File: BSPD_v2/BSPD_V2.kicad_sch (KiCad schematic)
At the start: 13 parts, among them K1 G5V-1, P1 0430450827, T1 T-BJT-NPN, U1 SN74HC00N, U2 LM393P, U3 LM393P, U4 LM393P, U5 SN74HC08N

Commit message: updated schematic
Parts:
- added C1, C2: C_Generic, Capacitor_THT:C_Disc_D12.5mm_W5.0mm_P10.00mm, symbol PCM_4ms_Capacitor:C_Generic
- added D1, D2, D3: LED, LED_THT:LED_D5.0mm_Horizontal_O6.35mm_Z9.0mm, symbol Device:LED
- added R1, R2, R3, R4, R5: R, PCM_Resistor_THT_AKL:R_Axial_DIN0918_L18.0mm_D9.0mm_P25.40mm_Horizontal, symbol Device:R
- added U6: LM2596T-5, PCM_Package_TO_SOT_THT_AKL:TO-220F-5_P3.4x2.06mm_StaggerEven_Lead1.86mm_Vertical, symbol Regulator_Switching:LM2596T-5
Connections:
- net +5V: now also U3.8 (VCC)
- net GND: now also P1.7, C1.2, C2.2, D1.1 (K), D2.1 (K), D3.1 (K)
- net at TRIM4.2 (Center): now also U4.3 (1IN+)
- net at U4.1 (1OUT): now also U5.5 (2B)
- net at U4.2 (1IN-): now also C1.1, R1.1
- net at U4.5 (2IN+): now also TRIM5.2 (Center)
- net at U4.6 (2IN-): now also C2.1, R2.1
- net at U4.7 (2OUT): now also U5.4 (2A)
- net IN: now reaches K1.10
- net at K1.2: now also T1.3 (E)
- net OUT: now reaches K1.5, K1.6
- net at U1.1 (1A): now also U2.1 (1OUT)
- net at U1.2 (1B): now also U3.1 (1OUT)
- net at U1.3 (1Y): now also R1.2
- net BPS_sensor: now reaches U3.2 (1IN-)
- net BPS_sensor: now also P1.2, U3.6 (2IN-), R4.2
- net at U3.5 (2IN+): now also TRIM3.2 (Center), U2.5 (2IN+)
- net at U3.7 (2OUT): now also U5.2 (1B)
- net TPS_sensor: now reaches P1.1
- net TPS_sensor: now also U2.2 (1IN-), U2.6 (2IN-), R5.2
- net at P1.8: now also U6.2 (OUT)
- net at T1.2 (B): now also U5.6 (2Y)
- net at U2.7 (2OUT): now also U5.1 (1A)
- net at U5.3 (1Y): now also R2.2
- new net: D3.2 (A), R3.1
- new net: D2.2 (A), R4.1
- new net: D1.2 (A), R5.1
- new net +12V: U6.1 (VIN)
- no-connect marks 0 -> 2
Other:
- moved on the sheet: P1, T1, TRIM2, TRIM3, TRIM4, TRIM5, U4, U5

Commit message: updated schematic
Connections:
- net GND: now also U6.3 (GND); no longer P1.7
- net at P1.8, U6.2 (OUT): now also R3.2
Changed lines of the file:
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@@
+	)
+	(junction
+		(at 45.72 175.26)
+		(diameter 0)
+		(color 0 0 0 0)
 	)
 	(junction
@@
 	(wire
 		(pts
-			(xy 43.18 173.99) (xy 43.18 175.26)
+			(xy 127 173.99) (xy 128.27 173.99)
 		)
 		(stroke
@@
 		(pts
 			(xy 66.04 181.61) (xy 66.04 194.31)
+		)
+		(stroke
+			(width 0)
+			(type default)
+		)
+	)
+	(wire
+		(pts
+			(xy 45.72 175.26) (xy 45.72 191.77)
 		)
 		(stroke
@@
 	(symbol
 		(lib_id "PCM_4ms_Power-symbol:GND")
-		(at 43.18 173.99 180)
+		(at 127 173.99 270)
 		(unit 1)
 		(exclude_from_sim no)
@@
 		(on_board yes)
 		(dnp no)
-		(fields_autoplaced yes)
 		(property "Reference" "#PWR026"
-			(at 43.18 167.64 0)
+			(at 120.65 173.99 0)
 			(effects
 				(font
@@
 		)
 		(property "Value" "GND"
-			(at 43.18 168.91 0)
+			(at 123.19 173.99 0)
 			(effects
 				(font
@@
 		)
 		(property "Footprint" ""
-			(at 43.18 173.99 0)
+			(at 127 173.99 0)
 			(effects
 				(font
@@
 		)
 		(property "Datasheet" ""
-			(at 43.18 173.99 0)
+			(at 127 173.99 0)
 			(effects
 				(font
@@
 		)
 		(property "Description" ""
-			(at 43.18 173.99 0)
+			(at 127 173.99 0)
 			(effects
 				(font
@@
 		)
 		(instances
-			(project ""
+			(project "BSPD_v2"
 				(path "/382198d7-19bb-422e-88d5-5462e049fe29"
 					(reference "#PWR026")

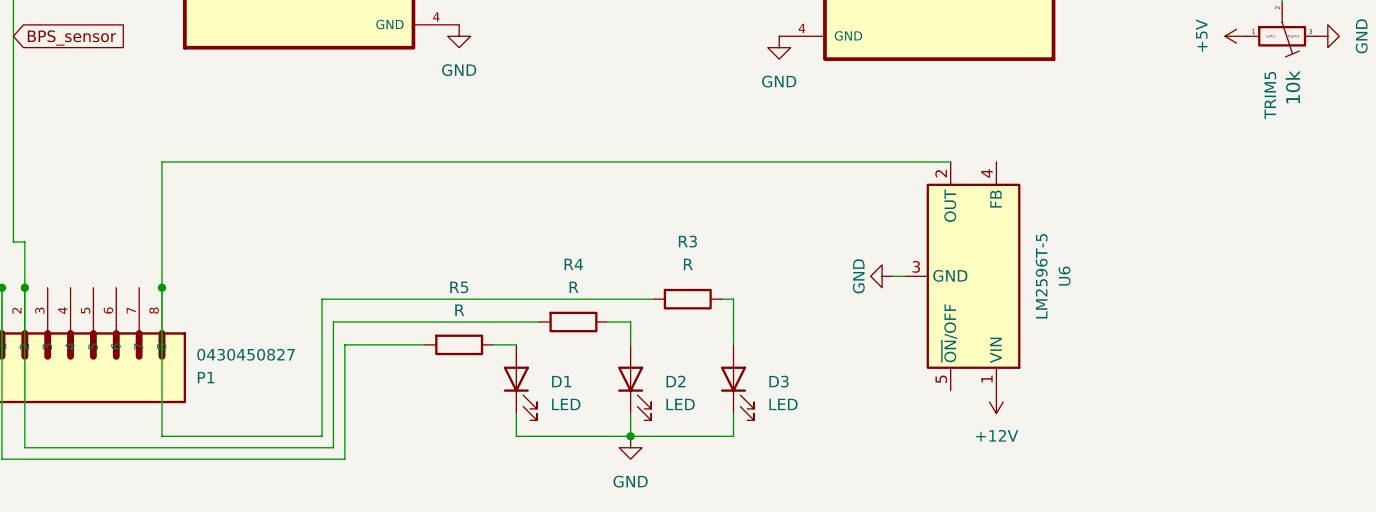
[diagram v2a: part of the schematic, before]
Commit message: updated footprints
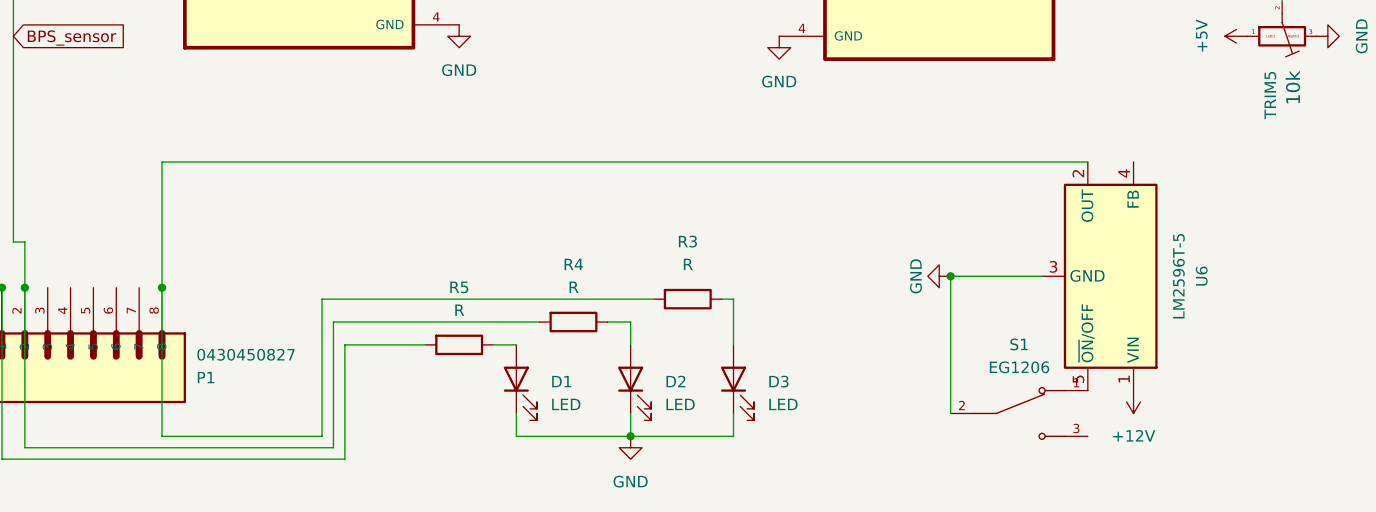
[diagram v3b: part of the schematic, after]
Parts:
- added S1: EG1206, Button_Switch_THT:SW_E-Switch_EG1224_SPDT_Angled, symbol EG1206_bspd:EG1206
- P1: footprint 0430450827:MOLEX_0430450827 -> Connector_Molex:Molex_Mega-Fit_76825-0008_2x04_P5.70mm_Horizontal
- T1: footprint (none) -> PCM_Package_TO_SOT_THT_AKL_OneLayer:TO-92L_ECB
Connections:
- net GND: now also S1.2
- net at U6.5 (~{ON}/OFF): now also S1.1
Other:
- moved on the sheet: U6
